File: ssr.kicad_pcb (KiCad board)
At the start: 2 copper layers, 99.1 x 76.2 mm, 34 parts, among them CON1 AVR-ISP-6, IC1 ATTINY44-SS, P1 CONN_4, P2 CONTACT, P3 CONTACT, P4 CONTACT, P5 CONTACT, P6 CONN_4, Q1 MOSFET_N, U1 MOC-3052, U2 TRIAC, U3 LTV-814

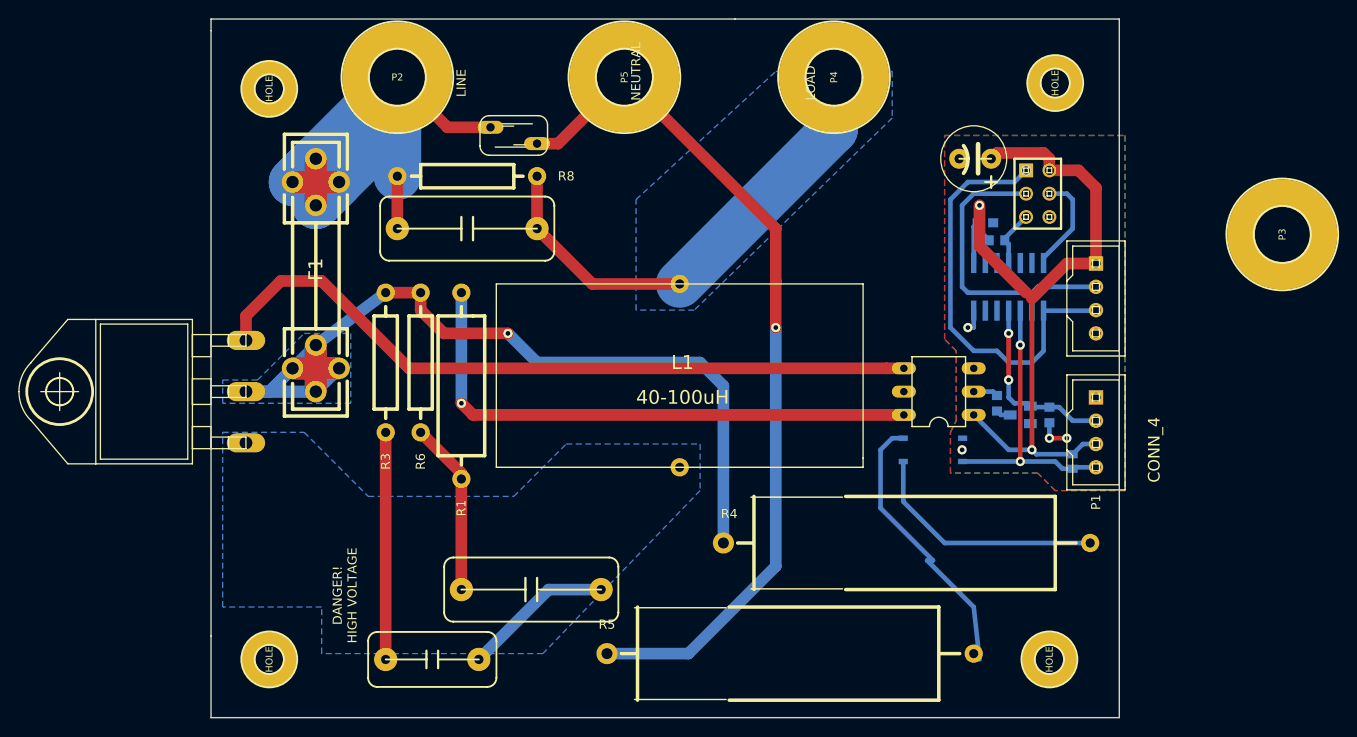
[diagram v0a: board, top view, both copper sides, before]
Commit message: one more rearrangement of parts creepage distances taken care of homogenized via sizes part names and values taken care of
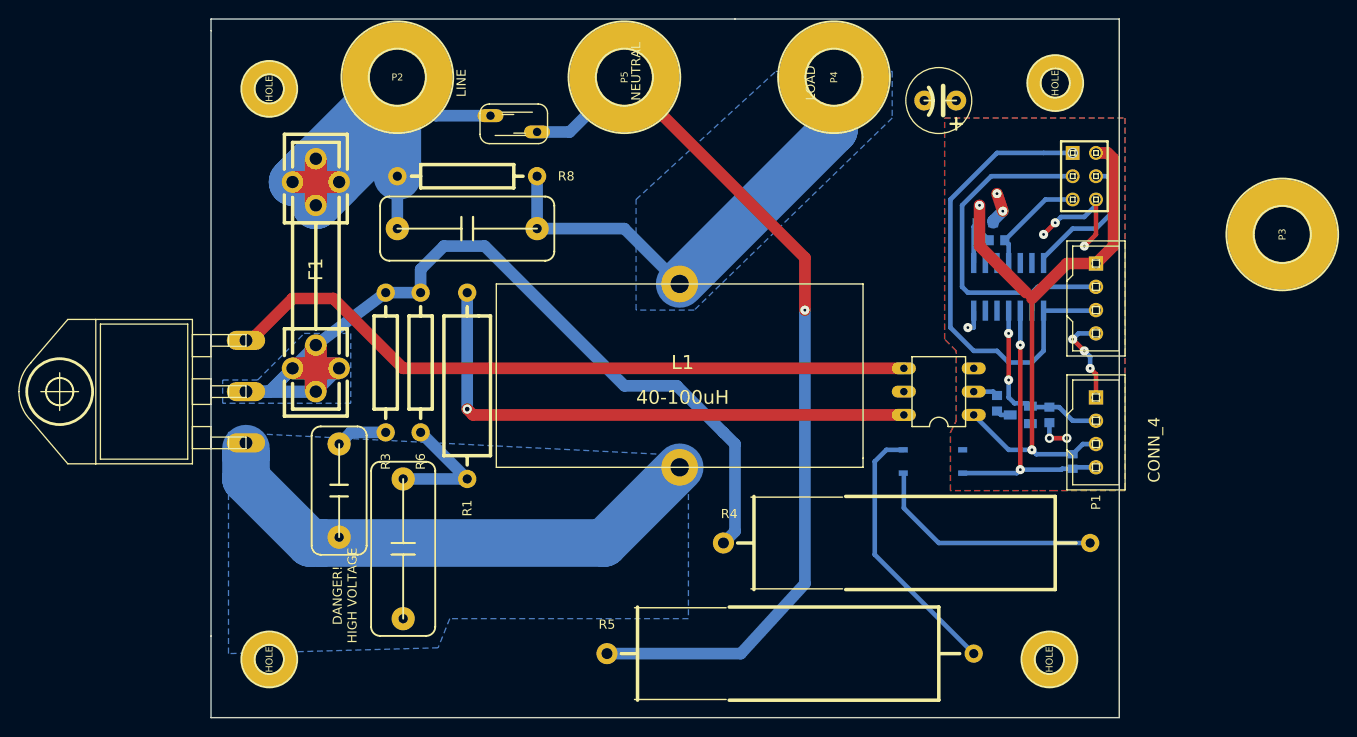
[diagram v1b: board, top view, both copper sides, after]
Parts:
- moved C1 21.0 mm to (113.7, 116.8), turned to 270 degrees
- moved C2 14.7 mm to (120.7, 123.2), turned to 270 degrees
- moved C5 7.41 mm to (179.1, 74.3)
- moved CON1 5.43 mm to (194.9, 82.5)
- moved VR1 1.27 mm to (132.7, 76.8)
- moved U3 1.27 mm to (178.4, 114.3)
- moved R1 0.64 mm to (127.6, 95.2)
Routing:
- net N-000002: track 16.5 -> 56.9 mm
- net GND: track 6.08 -> 33.3 mm, vias 3 -> 11
- net N-0000024: track 24.8 -> 5.61 mm
- net VCC: track 85.7 -> 77.8 mm
- net /RESET: track 6.16 -> 12.1 mm
- net /MISO: track 45.9 -> 51.8 mm
- net /SCK: track 33.5 -> 39.4 mm
- net /NEUTRAL: track 95.1 -> 100.3 mm
- net N-0000015: track 19.0 -> 14.2 mm
- net /MOSI: track 11.0 -> 15.6 mm
- net N-000003: track 79.9 -> 76.8 mm
- net /LINE: track 103.5 -> 106.2 mm, vias 1 -> 0
- net N-0000013: track 31.0 -> 29.1 mm
- net N-0000014: track 26.6 -> 25.7 mm
- net ZERO_CROSSING: track 31.4 -> 32.1 mm
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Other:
- net class hv added: clearance 2.54, trace_width 1.27, via_dia 1.016, via_drill 0.508

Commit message: this commit is a mess
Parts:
- moved C5 4.04 mm to (181.9, 77.2), turned to 90 degrees
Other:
- board text added: "GND"
- board text added: "ON"
- board text added: "SCL"
- board text added: "SDA"
- board text added: "TRIAC BLOC v.1.0"
- board text added: "VCC"
- board text added: "ZC"
- board text added: "mic@wemakethings.net CERN OHL v1.0 2013"
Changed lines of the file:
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@@
     (links 61)
     (no_connects 2)
-    (area 78.03896 54.56682 223.37014 141.68374)
+    (area 76.13396 51.39182 225.27514 142.43304)
     (thickness 1.6002)
-    (drawings 13)
-    (tracks 190)
+    (drawings 25)
+    (tracks 192)
     (zones 0)
     (modules 34)
@@
   )
   (setup
-    (last_trace_width 1.27)
+    (last_trace_width 0.508)
     (user_trace_width 0.508)
     (user_trace_width 1.27)
@@
     (uvia_min_drill 0.127)
     (pcb_text_width 0.29972)
-    (pcb_text_size 1.00076 1.00076)
+    (pcb_text_size 1.50114 1.50114)
     (mod_edge_width 0.14986)
     (mod_text_size 1.00076 1.00076)
     (mod_text_width 0.14986)
-    (pad_size 4.0005 4.0005)
-    (pad_drill 1.99898)
+    (pad_size 11.99896 11.99896)
+    (pad_drill 5.99948)
     (pad_to_mask_clearance 0)
     (aux_axis_origin 0 0)
@@
   )
   (module rc-master-CE-035X100 (layer F.Cu)
-    (at 179.07 74.295 180)
+    (at 181.864 77.216 90)
     (descr "POLCAP RADIAL")
     (tags "POLCAP RADIAL")
     (attr virtual)
-    (fp_text reference C5 (at 4.445 1.905 180) (layer B.SilkS)
+    (fp_text reference C5 (at 4.445 1.905 90) (layer B.SilkS)
       (effects (font (size 1.00076 1.00076) (thickness 0.14986)))
     )
-    (fp_text value 100uF (at 1.27 -2.54 180) (layer B.SilkS)
+    (fp_text value 100uF (at 1.27 -2.54 90) (layer B.SilkS)
       (effects (font (size 1.00076 1.00076) (thickness 0.14986)))
     )
@@
     (fp_arc (start 3.18516 -0.09906) (end 0.635 0) (angle 37.8) (layer F.SilkS) (width 0.4064))
     (fp_arc (start 2.9845 0.01016) (end 1.10998 1.42748) (angle 37.3) (layer F.SilkS) (width 0.4064))
-    (pad 1 thru_hole circle (at -1.905 0 180) (size 2.18186 2.18186) (drill 1.016)
+    (pad 1 thru_hole circle (at -1.905 0 90) (size 2.18186 2.18186) (drill 1.016)
       (layers *.Cu *.Mask F.Paste F.SilkS)
       (net 20 VCC)
     )
-    (pad 2 thru_hole circle (at 1.5875 0 180) (size 2.18186 2.18186) (drill 1.016)
+    (pad 2 thru_hole circle (at 1.5875 0 90) (size 2.18186 2.18186) (drill 1.016)
       (layers *.Cu *.Mask F.Paste F.SilkS)
       (net 7 GND)
@@
       (effects (font (size 1.00076 1.00076) (thickness 0.14986)))
     )
-    (fp_text value VR (at -22.225 0 360) (layer B.SilkS)
+    (fp_text value VR (at 1.397 5.207 360) (layer B.SilkS)
       (effects (font (size 1.27 1.27) (thickness 0.0889)))
     )
@@
     )
   )
-  (gr_text "DANGER!\nHIGH VOLTAGE" (at 114.3 128.27 90) (layer F.SilkS)
-    (effects (font (size 1.00076 1.00076) (thickness 0.25146)))
-  )
-  (gr_text LINE (at 127 72.39 90) (layer F.SilkS)
-    (effects (font (size 1.00076 1.00076) (thickness 0.25146)))
+  (gr_text LOAD (at 175.26 73.66 90) (layer F.SilkS)
+    (effects (font (size 1.50114 1.50114) (thickness 0.29972)))
+  )
+  (gr_text NEUTRAL (at 152.4 72.39 90) (layer F.SilkS)
+    (effects (font (size 1.50114 1.50114) (thickness 0.29972)))
+  )
+  (gr_text LINE (at 127 74.93 90) (layer F.SilkS)
+    (effects (font (size 1.50114 1.50114) (thickness 0.29972)))
+  )
+  (gr_text "mic@wemakethings.net\nCERN OHL v1.0 2013" (at 161.036 84.836) (layer F.SilkS)
+    (effects (font (size 1.50114 1.50114) (thickness 0.29972)))
+  )
+  (gr_text "TRIAC BLOC v.1.0" (at 161.036 81.788) (layer F.SilkS)
+    (effects (font (size 1.99898 1.99898) (thickness 0.29972)))
+  )
+  (gr_text GND (at 190.5 99.568) (layer F.SilkS)
+    (effects (font (size 1.50114 1.50114) (thickness 0.29972)))
+  )
+  (gr_text SDA (at 190.5 97.028) (layer F.SilkS)
+    (effects (font (size 1.50114 1.50114) (thickness 0.29972)))
+  )
+  (gr_text SCL (at 190.5 94.488) (layer F.SilkS)
+    (effects (font (size 1.50114 1.50114) (thickness 0.29972)))
+  )
+  (gr_text VCC (at 190.5 91.948) (layer F.SilkS)
+    (effects (font (size 1.50114 1.50114) (thickness 0.29972)))
+  )
+  (gr_text ZC (at 191.008 114.3) (layer F.SilkS)
+    (effects (font (size 1.50114 1.50114) (thickness 0.29972)))
+  )
+  (gr_text VCC (at 190.5 111.76) (layer F.SilkS)
+    (effects (font (size 1.50114 1.50114) (thickness 0.29972)))
+  )
+  (gr_text ON (at 191.008 109.22) (layer F.SilkS)
+    (effects (font (size 1.50114 1.50114) (thickness 0.29972)))
+  )
+  (gr_text GND (at 190.5 106.68) (layer F.SilkS)
+    (effects (font (size 1.50114 1.50114) (thickness 0.29972)))
+  )
+  (gr_text "DANGER!\nHIGH VOLTAGE" (at 130.556 127 90) (layer F.SilkS)
+    (effects (font (size 1.99898 1.99898) (thickness 0.25146)))
   )
   (gr_text NEUTRAL (at 146.05 71.12 90) (layer F.SilkS)
@@
   (segment (start 186.69 92.01658) (end 186.69 89.95664) (width 0.508) (layer B.Cu) (net 5))
   (segment (start 186.69 89.95664) (end 186.26836 89.535) (width 0.508) (layer B.Cu) (net 5))
-  (segment (start 189.23 95.25) (end 182.245 95.25) (width 0.508) (layer B.Cu) (net 6))
+  (segment (start 182.245 94.234) (end 182.245 93.98) (width 0.508) (layer B.Cu) (net 6))
+  (segment (start 181.61 85.725) (end 184.785 82.55) (width 0.508) (layer B.Cu) (net 6))
   (segment (start 184.785 82.55) (end 193.675 82.55) (width 0.508) (layer B.Cu) (net 6) (status 20))
-  (segment (start 181.61 85.725) (end 184.785 82.55) (width 0.508) (layer B.Cu) (net 6))
-  (segment (start 181.61 94.615) (end 181.61 85.725) (width 0.508) (layer B.Cu) (net 6))
-  (segment (start 182.245 95.25) (end 181.61 94.615) (width 0.508) (layer B.Cu) (net 6))
-  (segment (start 189.23 97.21342) (end 189.23 95.25) (width 0.508) (layer B.Cu) (net 6))
+  (segment (start 181.61 93.345) (end 181.61 85.725) (width 0.508) (layer B.Cu) (net 6))
+  (segment (start 182.245 93.98) (end 181.61 93.345) (width 0.508) (layer B.Cu) (net 6))
+  (segment (start 189.23 94.234) (end 182.245 94.234) (width 0.508) (layer B.Cu) (net 6))
+  (segment (start 182.245 94.234) (end 182.245 94.234) (width 0.508) (layer B.Cu) (net 6))
+  (segment (start 189.23 97.21342) (end 189.23 94.234) (width 0.508) (layer B.Cu) (net 6))
   (segment (start 189.865 94.615) (end 196.215 94.615) (width 0.508) (layer B.Cu) (net 6))
-  (segment (start 189.23 95.25) (end 189.865 94.615) (width 0.508) (layer B.Cu) (net 6))
+  (segment (start 189.23 94.234) (end 189.865 94.615) (width 0.508) (layer B.Cu) (net 6))
   (segment (start 196.215 99.695) (end 194.31 99.695) (width 0.508) (layer B.Cu) (net 7))
   (segment (start 196.215 104.14) (end 196.215 106.68) (width 0.508) (layer F.Cu) (net 7))
@@
     )
   )
-  (zone (net 0) (net_name "") (layer B.SilkS) (hatch edge 0.508)
+  (zone (net 0) (net_name "") (layer B.Mask) (hatch edge 0.508)
     (connect_pads (clearance 2.54))
-    (min_thickness 0.2032)
-    (fill (arc_segments 16) (thermal_gap 0.254) (thermal_bridge_width 0.508))
+    (min_thickness 0.254)
+    (fill (arc_segments 16) (thermal_gap 0.508) (thermal_bridge_width 0.508))
     (polygon
       (pts
-        (xy 149.86 111.76) (xy 152.4 111.76) (xy 153.67 113.665) (xy 153.67 115.57) (xy 144.145 125.095)
-        (xy 109.22 125.095) (xy 100.965 116.84) (xy 100.965 110.49) (xy 106.045 110.49) (xy 106.045 114.3)
-        (xy 111.125 119.38) (xy 141.605 119.38) (xy 149.225 111.76) (xy 149.86 111.76)
+        (xy 173.228 72.644) (xy 173.228 76.708) (xy 152.4 97.028) (xy 146.304 97.028) (xy 145.796 97.028)
+        (xy 145.796 85.344) (xy 161.544 70.612) (xy 173.228 72.644)
       )
     )
   )
-  (zone (net 0) (net_name "") (layer B.SilkS) (hatch edge 0.508)
+  (zone (net 0) (net_name "") (layer B.Mask) (hatch edge 0.508)
     (connect_pads (clearance 2.54))
-    (min_thickness 0.2032)
-    (fill (arc_segments 16) (thermal_gap 0.254) (thermal_bridge_width 0.508))
+    (min_thickness 0.254)
+    (fill (arc_segments 16) (thermal_gap 0.508) (thermal_bridge_width 0.508))
     (polygon
       (pts
-        (xy 173.355 72.39) (xy 173.355 76.835) (xy 152.4 97.155) (xy 146.05 97.155) (xy 146.05 85.09)
-        (xy 161.29 71.12) (xy 173.355 71.12) (xy 173.355 72.39)
+        (xy 149.352 111.76) (xy 152.4 111.76) (xy 153.924 113.284) (xy 153.924 115.316) (xy 144.272 124.968)
+        (xy 109.22 124.968) (xy 101.092 116.84) (xy 101.092 110.744) (xy 101.092 110.236) (xy 106.172 110.236)
+        (xy 106.172 114.3) (xy 111.252 119.38) (xy 141.224 119.38) (xy 149.352 111.76)
       )
     )
-  )
-  (zone (net 0) (net_name "") (layer B.SilkS) (hatch edge 0.508)
-    (connect_pads (clearance 2.54))
-    (min_thickness 0.2032)
-    (fill (arc_segments 16) (thermal_gap 0.254) (thermal_bridge_width 0.508))
-    (polygon
-      (pts
-        (xy 114.935 104.14) (xy 111.125 107.315) (xy 100.965 107.315) (xy 100.965 104.775) (xy 104.775 104.775)
-        (xy 109.855 99.695) (xy 111.76 99.695) (xy 114.935 102.87)
-      )
-    )
-  )
-  (zone (net 0) (net_name "") (layer B.SilkS) (hatch edge 0.508)
-    (connect_pads (clearance 2.54))
-    (min_thickness 0.2032)
-    (fill (arc_segments 16) (thermal_gap 0.254) (thermal_bridge_width 0.508))
-    (polygon
-      (pts
-        (xy 123.19 76.2) (xy 111.76 87.63) (xy 110.49 87.63) (xy 106.68 84.455) (xy 106.045 81.915)
-        (xy 114.3 73.66)
-      )
-    )
